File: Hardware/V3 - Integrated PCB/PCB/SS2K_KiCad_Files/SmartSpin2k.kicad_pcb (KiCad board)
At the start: 2 copper layers, 57.2 x 60.3 mm, 84 parts, among them J1 B4B-XH-AMLFSN, J2 B4B-XH-AMLFSN, J3 B8B-XH-A_LFSN, J4 10118194-0001LF, Q1 S8050, Q2 S8050, SW1 SW_Push, SW2 SW_Push, U1 ESP32-WROOM-32D, U2 TMC2209-LA-T, U3 MAX3232, U4 TPS5430DDA, U5 INTERFACE-CP2102-GMR(QFN28), U6 LM1117-3.3

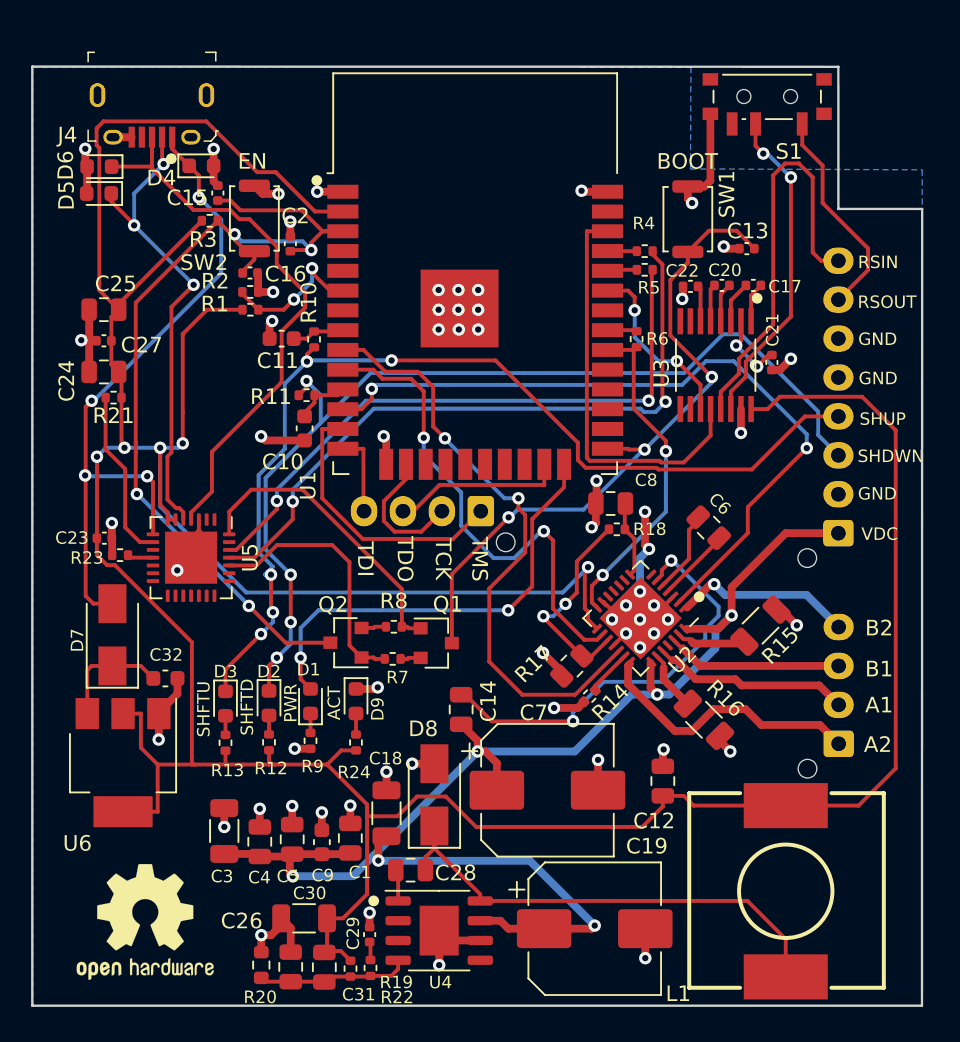
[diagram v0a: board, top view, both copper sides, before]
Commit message: Fixed Transistor Footprint, Added new Switch, Chamfered corners
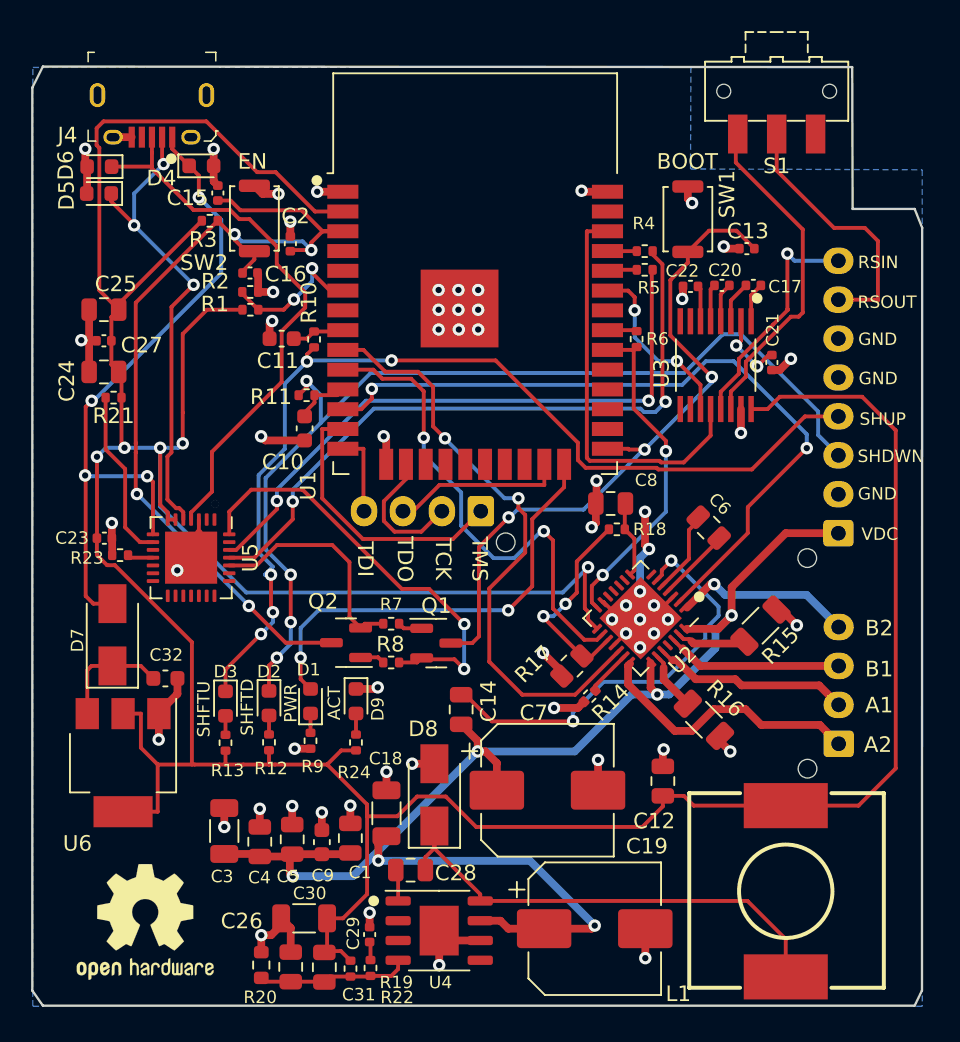
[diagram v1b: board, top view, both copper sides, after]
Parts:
- S1: footprint Button_Switch_SMD:SW_SPDT_PCM12 -> Button_Switch_SMD:SW_SPDT_CK-JS102011SAQN
- moved R8 2.30 mm to (144.4, 126.9)
- moved R7 2.26 mm to (144.4, 124.4)
- moved S1 0.90 mm to (169.1, 90.2)
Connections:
- Q1 pad 1: /DTR -> Net-(Q1-Pad1)
- Q1 pad 2: Net-(Q1-Pad2) -> /DTR
- Q2 pad 1: /RTS -> Net-(Q2-Pad1)
- Q2 pad 2: Net-(Q2-Pad2) -> /RTS
- R7 pad 1: Net-(Q1-Pad2) -> Net-(Q1-Pad1)
- R8 pad 2: Net-(Q2-Pad2) -> Net-(Q2-Pad1)
- S1 pad 1: /RS232OUT1 -> unconnected-(S1-Pad1)
- S1 pad 2: Net-(S1-Pad2) -> /RS232OUT1
- S1 pad 3: unconnected-(S1-Pad3) -> Net-(S1-Pad3)
- U3 pad 14: Net-(S1-Pad2) -> Net-(S1-Pad3)
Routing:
- net Net-(S1-Pad3): track 0.00 -> 21.6 mm
- net Net-(S1-Pad2): track 21.0 -> 0.00 mm, vias 2 -> 0
- net /RS232IN1: track 26.3 -> 15.3 mm, vias 0 -> 1
- net /DTR: track 19.5 -> 28.2 mm, vias 0 -> 2
- net GND: track 96.4 -> 90.5 mm
- net /RS232OUT1: track 13.8 -> 17.1 mm
- net /RTS: track 16.7 -> 14.8 mm
- net Net-(Q2-Pad2): track 1.60 -> 0.00 mm
- net Net-(Q2-Pad1): track 0.00 -> 1.60 mm
- net Net-(Q1-Pad1): track 0.00 -> 1.57 mm
- net Net-(Q1-Pad2): track 1.32 -> 0.00 mm
- net /IO0_BOOT: track 43.9 -> 44.7 mm
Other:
- outline, holes or cut-outs redrawn

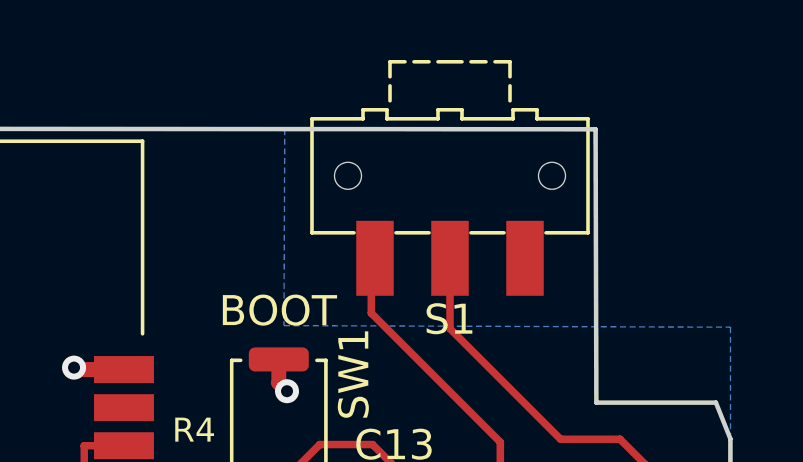
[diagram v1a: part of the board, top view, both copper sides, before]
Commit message: Updated build files and .step for CAD
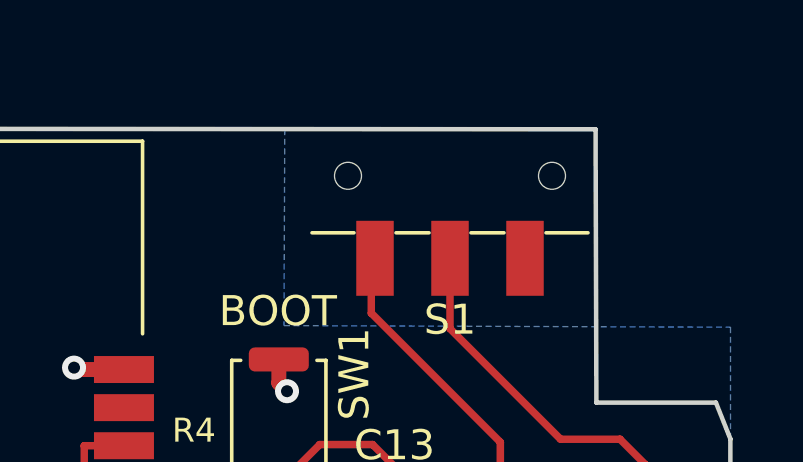
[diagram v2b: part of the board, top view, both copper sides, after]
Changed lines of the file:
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@@
     )
     (fp_line (start 2 3.3) (end 2 3.3) (layer "F.SilkS") (width 0.12))
-    (fp_line (start 2 3.8) (end 1.5 3.8) (layer "F.SilkS") (width 0.12))
-    (fp_line (start 4.6 -1.9) (end 4.6 1.9) (layer "F.SilkS") (width 0.12))
-    (fp_line (start -2.1 1.9) (end -2.1 2.2) (layer "F.SilkS") (width 0.12))
-    (fp_line (start 2 3.8) (end 2 3.3) (layer "F.SilkS") (width 0.12))
-    (fp_line (start -2 3.8) (end -2 3.3) (layer "F.SilkS") (width 0.12))
-    (fp_line (start -2 3.8) (end -1.5 3.8) (layer "F.SilkS") (width 0.12))
-    (fp_line (start -2.9 2.2) (end -2.9 1.9) (layer "F.SilkS") (width 0.12))
-    (fp_line (start -0.4 2.2) (end -0.4 1.9) (layer "F.SilkS") (width 0.12))
-    (fp_line (start -2.1 2.2) (end -2.9 2.2) (layer "F.SilkS") (width 0.12))
     (fp_line (start 0.7 3.8) (end 0.7 3.8) (layer "F.SilkS") (width 0.12))
-    (fp_line (start 2.1 1.9) (end 0.4 1.9) (layer "F.SilkS") (width 0.12))
-    (fp_line (start -4.6 1.9) (end -4.6 -1.9) (layer "F.SilkS") (width 0.12))
-    (fp_line (start 0.4 3.8) (end -0.4 3.8) (layer "F.SilkS") (width 0.12))
     (fp_line (start 1.8 -1.9) (end 0.7 -1.9) (layer "F.SilkS") (width 0.12))
     (fp_line (start 0.7 -1.9) (end 0.7 -1.9) (layer "F.SilkS") (width 0.12))
     (fp_line (start 3.2 -1.9) (end 4.6 -1.9) (layer "F.SilkS") (width 0.12))
-    (fp_line (start 2.9 1.9) (end 2.9 2.2) (layer "F.SilkS") (width 0.12))
     (fp_line (start -0.7 3.8) (end -0.7 3.8) (layer "F.SilkS") (width 0.12))
     (fp_line (start -2 2.5) (end -2 2.5) (layer "F.SilkS") (width 0.12))
     (fp_line (start -0.7 -1.9) (end -1.8 -1.9) (layer "F.SilkS") (width 0.12))
-    (fp_line (start 0.4 2.2) (end -0.4 2.2) (layer "F.SilkS") (width 0.12))
-    (fp_line (start 1.5 3.8) (end 1.5 3.8) (layer "F.SilkS") (width 0.12))
     (fp_line (start -1.8 -1.9) (end -1.8 -1.9) (layer "F.SilkS") (width 0.12))
-    (fp_line (start -0.4 1.9) (end -2.1 1.9) (layer "F.SilkS") (width 0.12))
-    (fp_line (start 2.1 2.2) (end 2.1 1.9) (layer "F.SilkS") (width 0.12))
-    (fp_line (start 1.2 3.8) (end 0.7 3.8) (layer "F.SilkS") (width 0.12))
     (fp_line (start -4.6 -1.9) (end -3.2 -1.9) (layer "F.SilkS") (width 0.12))
-    (fp_line (start 0.4 1.9) (end 0.4 2.2) (layer "F.SilkS") (width 0.12))
-    (fp_line (start -1.2 3.8) (end -0.7 3.8) (layer "F.SilkS") (width 0.12))
-    (fp_line (start -2 3) (end -2 2.5) (layer "F.SilkS") (width 0.12))
     (fp_line (start -2 3.3) (end -2 3.3) (layer "F.SilkS") (width 0.12))
     (fp_line (start -0.4 3.8) (end -0.4 3.8) (layer "F.SilkS") (width 0.12))
     (fp_line (start 2 2.5) (end 2 2.5) (layer "F.SilkS") (width 0.12))
-    (fp_line (start -2.9 1.9) (end -4.6 1.9) (layer "F.SilkS") (width 0.12))
-    (fp_line (start 2 3) (end 2 2.5) (layer "F.SilkS") (width 0.12))
     (fp_line (start -4.6 1.9) (end -4.6 1.9) (layer "F.SilkS") (width 0.12))
-    (fp_line (start 4.6 1.9) (end 2.9 1.9) (layer "F.SilkS") (width 0.12))
-    (fp_line (start 2.9 2.2) (end 2.1 2.2) (layer "F.SilkS") (width 0.12))
     (fp_line (start -1.5 3.8) (end -1.5 3.8) (layer "F.SilkS") (width 0.12))
     (fp_line (start 3.25 2.25) (end 5 2.25) (layer "F.CrtYd") (width 0.05))
@@
     (pad "3" smd rect (at 2.5 -2.75 180) (size 1.25 2.5) (layers "F.Cu" "F.Paste" "F.Mask")
       (net 111 "Net-(S1-Pad3)") (pintype "passive"))
-    (model "${KICAD6_3DMODEL_DIR}/Button_Switch_SMD.3dshapes/SW_SPDT_CK-JS102011SAQN.wrl"
+    (model "${KIPRJMOD}/3d_Parts/JS102011SAQN.step"
       (offset (xyz 0 0 0))
       (scale (xyz 1 1 1))
-      (rotate (xyz 0 0 0))
+      (rotate (xyz 90 180 180))
     )
   )
@@
     (property "Sheetfile" "SmartSpin2k.kicad_sch")
     (property "Sheetname" "")
-    (attr through_hole)
+    (attr through_hole exclude_from_bom)
     (fp_text reference "J1" (at 3.75 3.55 90) (layer "B.SilkS")
       (effects (font (size 1 1) (thickness 0.15)) (justify mirror))
@@
     (property "Sheetfile" "SmartSpin2k.kicad_sch")
     (property "Sheetname" "")
-    (attr through_hole)
+    (attr through_hole exclude_from_bom)
     (fp_text reference "J3" (at 8.66 3.355 90) (layer "B.SilkS")
       (effects (font (size 1 1) (thickness 0.15)) (justify mirror))
@@
     (property "Sheetfile" "SmartSpin2k.kicad_sch")
     (property "Sheetname" "")
-    (attr through_hole)
+    (attr through_hole exclude_from_bom)
     (fp_text reference "J2" (at 3.75 3.55) (layer "B.SilkS")
       (effects (font (size 1 1) (thickness 0.15)) (justify mirror))

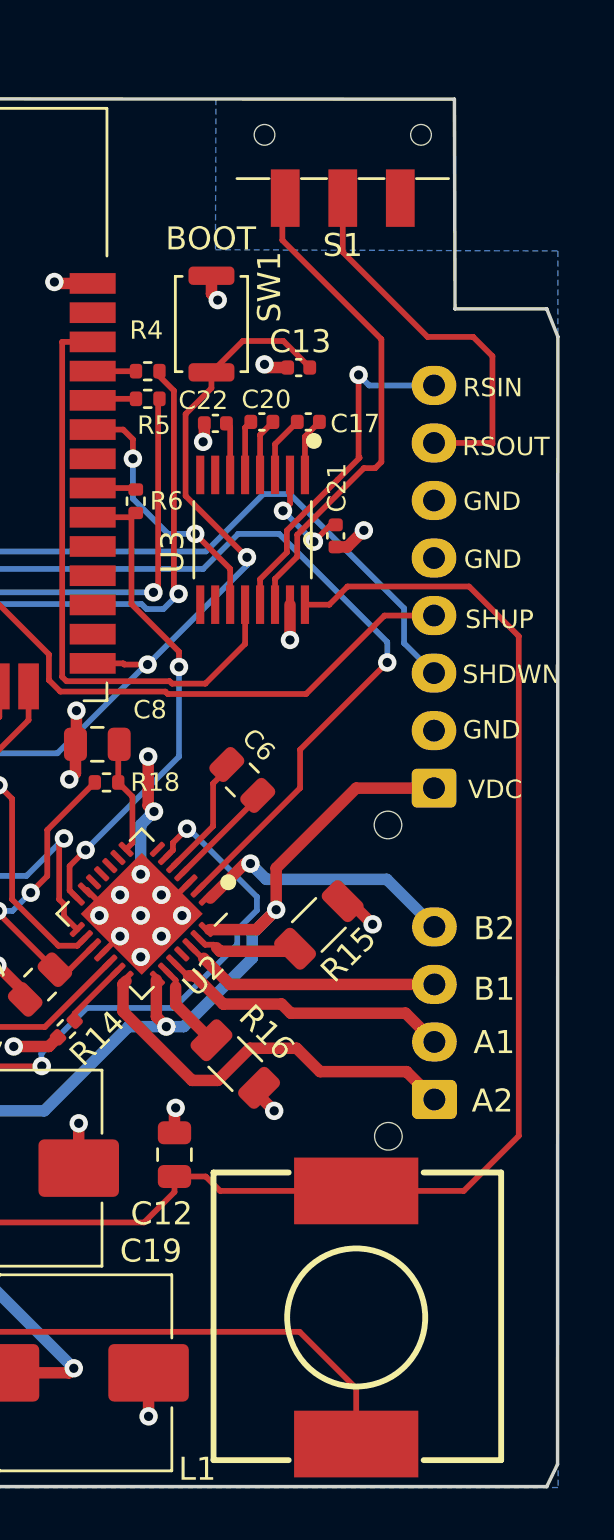
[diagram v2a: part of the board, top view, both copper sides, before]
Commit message: Updated PCB
Moved Switch Back
Switched A1 & A2 on Motor Jumper
Rotated back Silkscreen images
Added Silkscreen to Jumpers on back
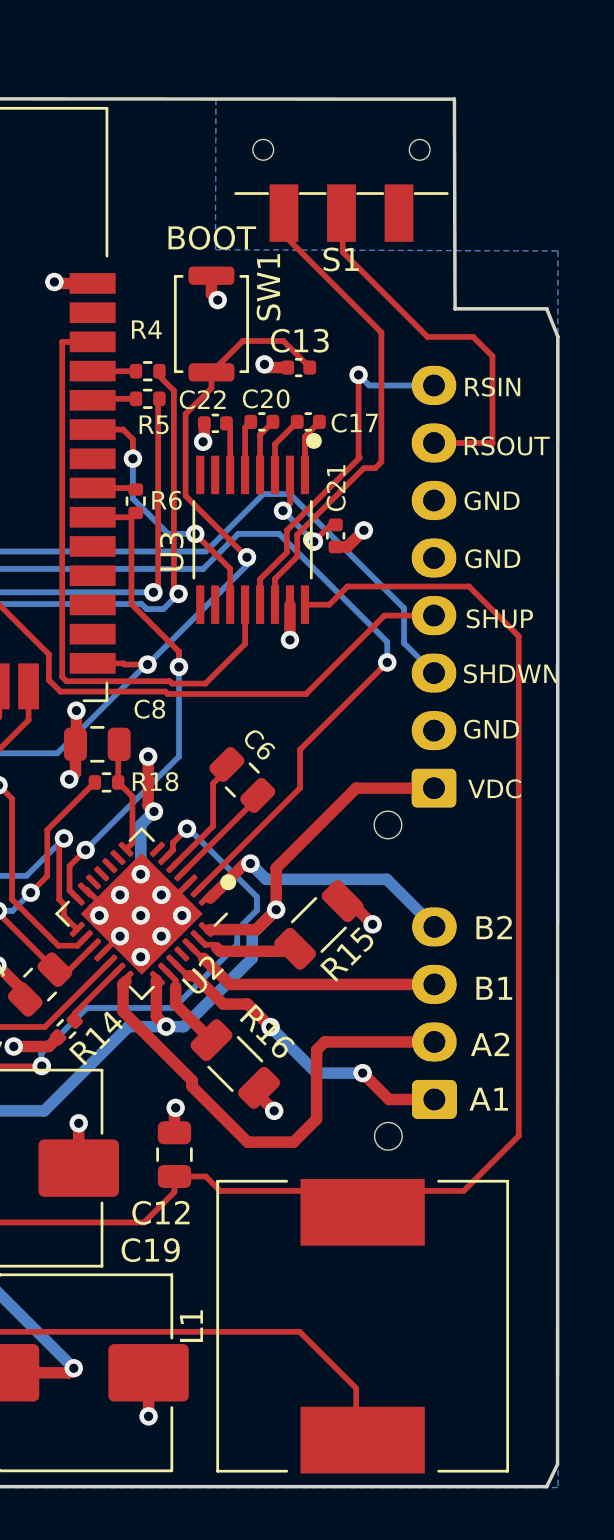
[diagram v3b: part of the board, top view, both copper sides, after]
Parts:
- L1: value 15uH(Iron_Core) -> L_Iron; footprint Inductor_SMD_Extra:L_SXN_SMDRI127_150MT -> Inductor_SMD:L_12x12mm_H8mm
- moved L1 7.91 mm to (170.0, 142.0)
- moved S1 0.65 mm to (169.1, 90.9)
- turned G*** to 0 degrees
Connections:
- J1 pad 1: /A2 -> /A1
- J1 pad 2: /A1 -> /A2
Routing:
- net /A2: track 17.8 -> 21.1 mm
- net /A1: track 12.8 -> 13.8 mm, vias 0 -> 2
- net Net-(S1-Pad3): track 21.6 -> 20.9 mm
- net /RS232OUT1: track 17.1 -> 16.4 mm
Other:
- board text added: "Ground"
- board text added: "JTAG"
- board text added: "RS 232 In"
- board text added: "RS232 Out"
- board text added: "Shift Down"
- board text added: "Shift Up"
